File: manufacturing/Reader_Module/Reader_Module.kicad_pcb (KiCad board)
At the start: 4 copper layers, 30 x 70 mm, 49 parts, among them J1 SW-Debug, J2 Conn_01x04_Pin, SW1 NRST, U1 STM32L431KBU6, U2 SN65HVD230, U3 USBLC6-2, Y1 13.56MHz

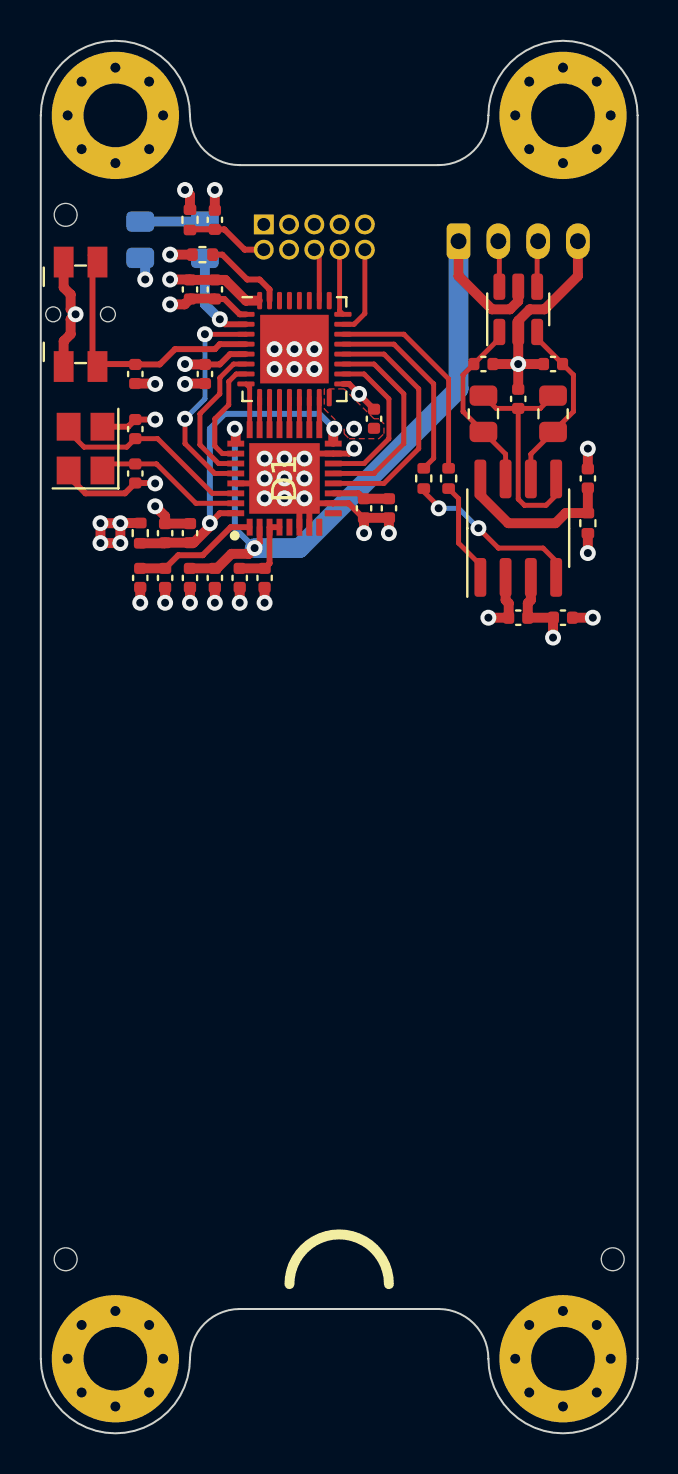
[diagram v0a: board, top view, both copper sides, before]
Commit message: Update PCB
Added Supplyline filtering
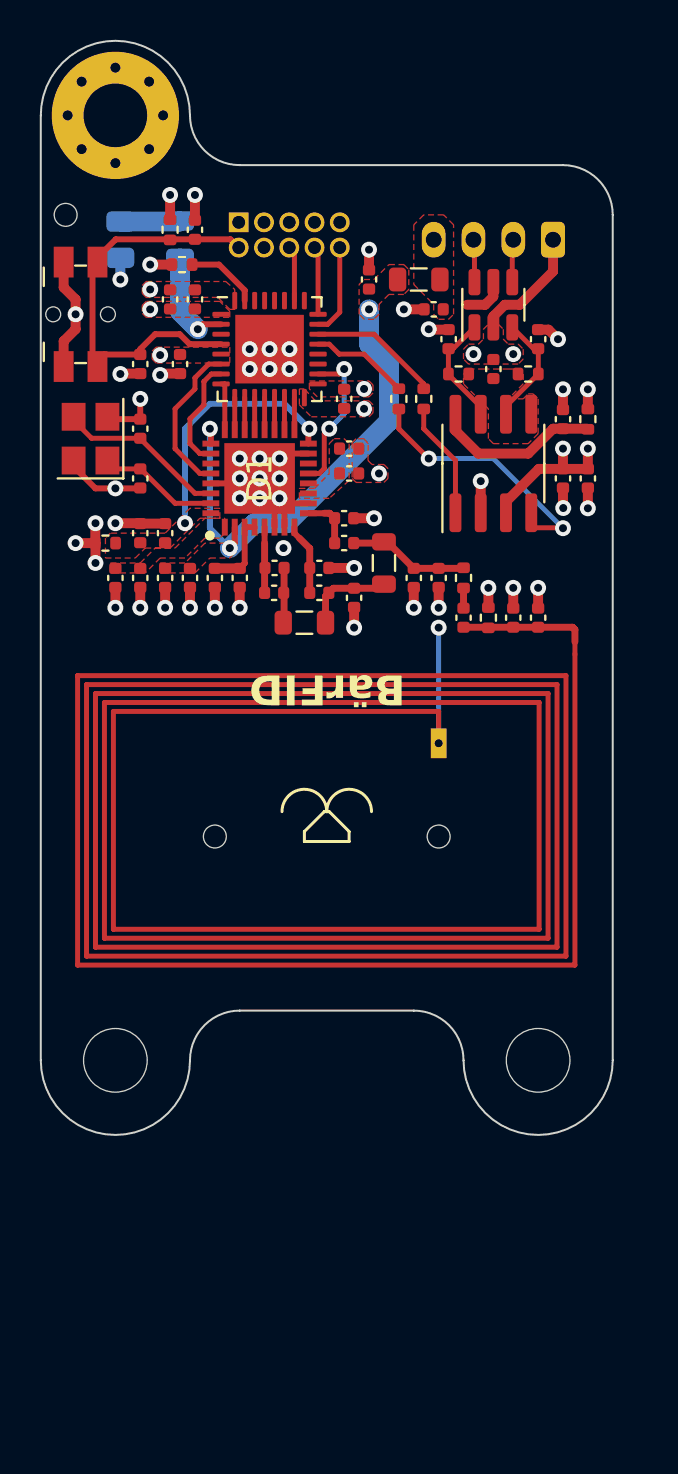
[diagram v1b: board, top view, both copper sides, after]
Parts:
- removed H2: MountingHole_Pad, MountingHole:MountingHole_3.2mm_M3_Pad_Via
- added AE1: Antenna_Loop, RF_Antenna:Custom_RFID_1, F.Cu at (109.3, 86.5)
- added C25: 47p, Capacitor_SMD:C_0402_1005Metric, F.Cu at (132.5, 84.0)
- added C26: 27p, Capacitor_SMD:C_0402_1005Metric, F.Cu at (131.2, 84.0)
- added C27: 68p, Capacitor_SMD:C_0402_1005Metric, F.Cu at (128.8, 84.0)
- added C28: 2u2, Capacitor_SMD:C_0402_1005Metric, F.Cu at (124.0, 67.0)
- added C29: 2u2, Capacitor_SMD:C_0402_1005Metric, F.Cu at (127.2, 68.5)
- added C30: 1n5, Capacitor_SMD:C_0402_1005Metric, F.Cu at (119.2, 81.5)
- added C31: 1n5, Capacitor_SMD:C_0402_1005Metric, F.Cu at (119.2, 82.8)
- added C32: 1n2, Capacitor_SMD:C_0402_1005Metric, F.Cu at (121.5, 82.8)
- added C33: 1n2, Capacitor_SMD:C_0402_1005Metric, F.Cu at (121.5, 81.5)
- added C34: 680p, Capacitor_SMD:C_0402_1005Metric, F.Cu at (123.2, 83.0)
- added C35: 220p, Capacitor_SMD:C_0402_1005Metric, F.Cu at (122.8, 80.2)
- added C36: 680p, Capacitor_SMD:C_0402_1005Metric, F.Cu at (122.8, 79.0)
- added C37: 100p, Capacitor_SMD:C_0402_1005Metric, F.Cu at (126.2, 82.0)
- added C38: 47p, Capacitor_SMD:C_0402_1005Metric, F.Cu at (127.5, 82.0)
- added FB2: 100 @ 100MHz, Inductor_SMD:L_0805_2012Metric, F.Cu at (126.5, 67.0)
- added G***: LOGO, Symbol:RFID-Gwent_M, B.Cu at (122.0, 98.5)
- added L1: 150n, Inductor_SMD:L_0805_2012Metric, F.Cu at (120.8, 84.2)
- added L2: 150n, Inductor_SMD:L_0805_2012Metric, F.Cu at (124.8, 81.2)
- added R10: 680R, Resistor_SMD:R_0402_1005Metric, F.Cu at (130.0, 84.0)
- added R11: 0R, Resistor_SMD:R_0402_1005Metric, F.Cu at (128.8, 82.0)
- H3, H4: footprint MountingHole:MountingHole_3.2mm_M3_Pad_Via -> MountingHole:MountingHole_3.2mm_M3
- J2: footprint Connector_Molex:Molex_Micro-Latch_53253-0470_1x04_P2.00mm_Vertical -> Connector_Molex:Molex_Micro-Latch_53254-0470_1x04_P2.00mm_Horizontal
- R6, R8: footprint Resistor_SMD:R_0805_2012Metric -> Resistor_SMD:R_0402_1005Metric
- moved H6 23.0 mm to (127.5, 95.0)
- moved H5 22.5 mm to (116.2, 95.0)
- moved H3 15.1 mm to (132.5, 106.2)
- moved H4 15.0 mm to (111.2, 106.2)
- moved C20 7.35 mm to (133.8, 77.0), turned to -90 degrees
- moved C19 7.11 mm to (135.0, 77.0), turned to -90 degrees
- moved R9 5.23 mm to (135.0, 74.0), turned to 90 degrees
- moved J2 4.75 mm to (133.2, 65.0), turned to 180 degrees
- moved R5 4.19 mm to (126.8, 73.0)
- moved R7 4.19 mm to (125.5, 73.0)
- moved C5 3.61 mm to (123.0, 75.5), turned to 180 degrees
- moved U2 3.48 mm to (130.2, 76.2)
- moved C24 3.23 mm to (133.8, 74.0)
- moved R6 2.36 mm to (128.5, 71.8), turned to 180 degrees
- moved R8 2.36 mm to (132.0, 71.8), turned to 180 degrees
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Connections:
- D1 pad 12: /MCU/TRF_ASK_OOK -> unconnected-(D1-ASK/OOK-Pad12)
- D1 pad 14: /MCU/TRF_MOD -> /TRF/TRF_MOD
- D1 pad 27: /MCU/TRF_SYS_CLK -> unconnected-(D1-SYS_CLK-Pad27)
- J2 pad 1: +5V -> GND
- J2 pad 2: /CAN/CAN_CON+ -> /CAN/CAN_CON-
- J2 pad 3: /CAN/CAN_CON- -> /CAN/CAN_CON+
- J2 pad 4: GND -> /CAN/CONN_5V
- U1 pad 18: /MCU/TRF_MOD -> /MCU/TRF_IRQ
- U1 pad 19: /MCU/TRF_IRQ -> unconnected-(U1-PA9-Pad19)
- U1 pad 20: /MCU/TRF_ASK_OOK -> unconnected-(U1-PA10-Pad20)
- U1 pad 3: /MCU/TRF_EN -> unconnected-(U1-PC15-Pad3)
- U1 pad 6: /MCU/TRF_SYS_CLK -> /MCU/TRF_EN
- U3 pad 5: +5V -> /CAN/CONN_5V
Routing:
- net +5V: track 39.9 -> 25.0 mm, vias 2 -> 3
- net /MCU/TRF_ASK_OOK: track 12.6 -> 0.00 mm
- net /CAN/VREF: track 11.7 -> 0.00 mm
- net +3V3: track 21.0 -> 12.7 mm
- net /MCU/TRF_MOD: track 8.15 -> 0.00 mm
- net /MCU/TRF_SYS_CLK: track 7.57 -> 0.00 mm
- net /TRF/VDD_A: track 6.36 -> 0.00 mm
- net /PCB Antenna/Antenna: track 0.00 -> 6.26 mm
- net Net-(C35-Pad2): track 0.00 -> 6.06 mm
- net /TRF/VDD_X: track 18.5 -> 12.8 mm
- net /CAN/CAN_RX: track 9.84 -> 4.99 mm
- net Net-(U2-R): track 9.04 -> 13.6 mm
- net Net-(C32-Pad2): track 0.00 -> 4.52 mm
- net /CAN/CAN_TX: track 10.6 -> 6.59 mm
- net /Matching NW/RF_RX_IN1: track 0.00 -> 3.62 mm
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- added copper zone on F.Cu, net +3V3
- added copper zone on F.Cu, net +5V
- added copper zone on F.Cu, net /CAN/CONN_5V
- added copper zone on F.Cu, net /CAN/VREF
- added copper zone on F.Cu, net /TRF/BG
- added copper zone on F.Cu, net /TRF/VDD_A
- added copper zone on F.Cu, net /TRF/VDD_X
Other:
- board size 30 x 70 mm -> 28.8 x 55 mm
- board text added: "-"
- board text added: "BärFID"

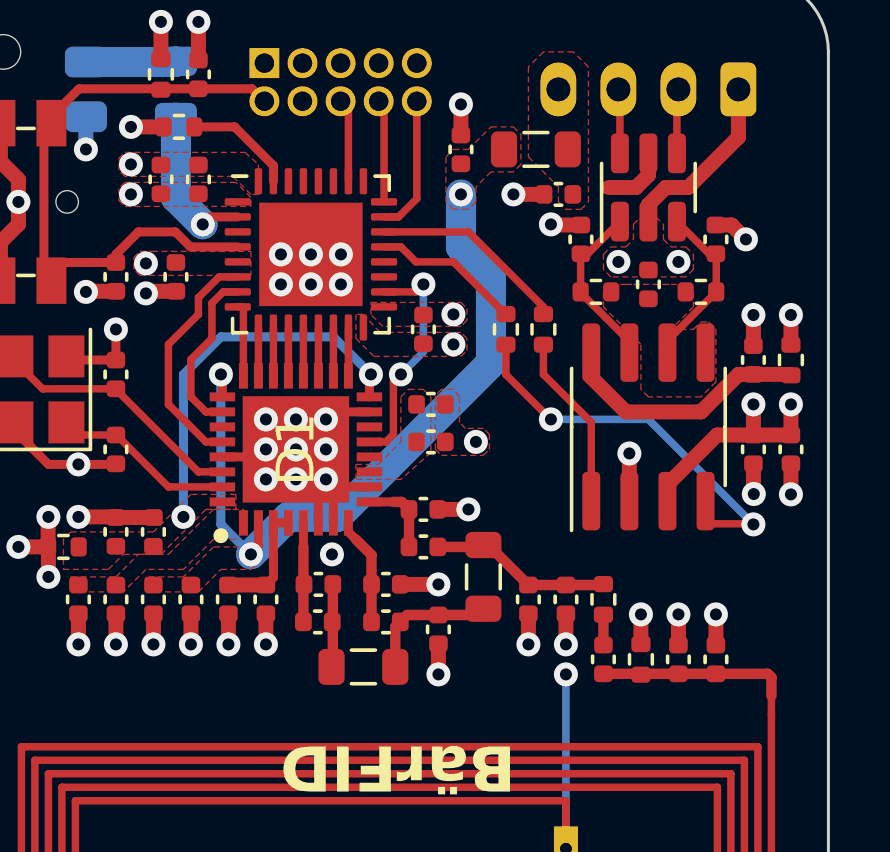
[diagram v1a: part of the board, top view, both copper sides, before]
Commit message: added PCB Images
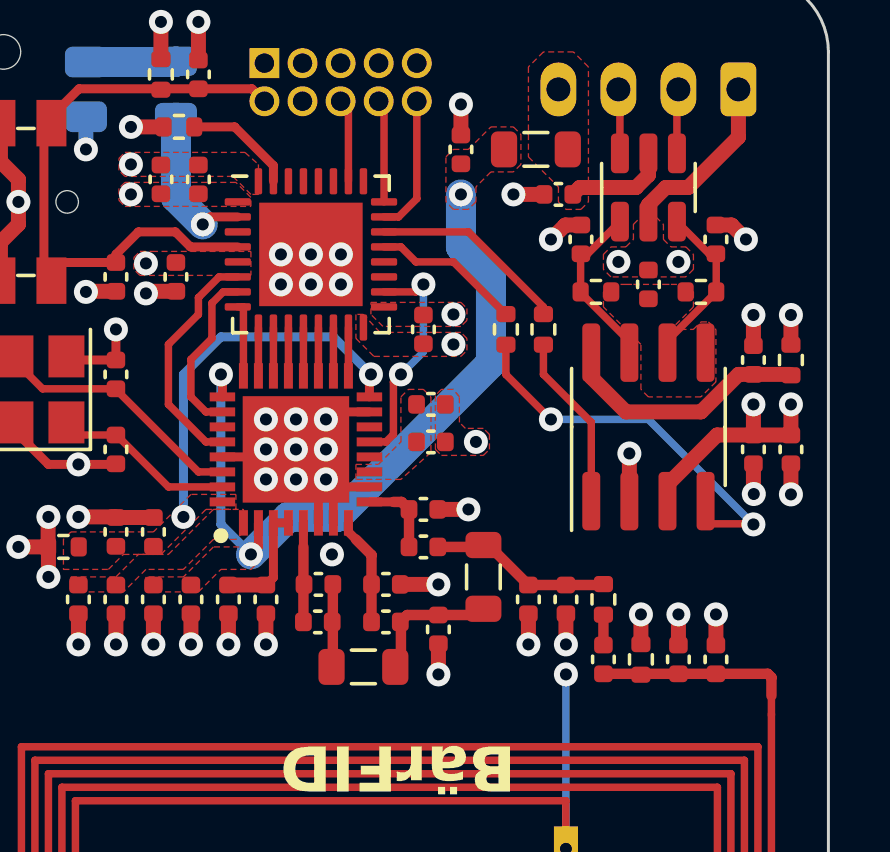
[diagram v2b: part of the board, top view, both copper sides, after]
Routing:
- net /CAN/CONN_5V: track 2.22 -> 3.51 mm
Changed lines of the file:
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@@
     (property "ki_description" "TRF7964A Multi Protocol Fully Integrated 13.56-MHz NFC / RFID Reader/Writer IC")
     (attr smd)
-    (fp_text reference "D1" (at 0 0 90) (layer "F.SilkS")
+    (fp_text reference "D1" (at 0 0 90) (layer "F.SilkS") hide
         (effects (font (size 1.27 1.27) (thickness 0.254)))
     )
@@
     )
   )
+  (segment (start 128 69.52) (end 127.48 69.52) (width 0.5) (layer "F.Cu") (net 1))
   (segment (start 135 77.48) (end 135 78.5) (width 0.5) (layer "F.Cu") (net 1))
   (segment (start 133.75 77.48) (end 133.75 78.474694) (width 0.5) (layer "F.Cu") (net 1))
@@
   (segment (start 132.5 83.52) (end 132.5 82.5) (width 0.5) (layer "F.Cu") (net 1))
   (segment (start 133.75 78.474694) (end 133.762653 78.487347) (width 0.5) (layer "F.Cu") (net 1))
-  (segment (start 127.020004 69.52) (end 127.000004 69.5) (width 0.5) (layer "F.Cu") (net 1))
   (segment (start 129.615 78.725) (end 129.615 77.135018) (width 0.5) (layer "F.Cu") (net 1))
-  (segment (start 132.5 69.52) (end 133.02 69.52) (width 0.5) (layer "F.Cu") (net 1))
   (segment (start 109.25 69.5) (end 109.25 68.75) (width 0.5) (layer "F.Cu") (net 1))
-  (segment (start 133.02 69.52) (end 133.5 70) (width 0.5) (layer "F.Cu") (net 1))
   (segment (start 120.95 75.75) (end 119.75 75.75) (width 0.3) (layer "F.Cu") (net 1))
   (segment (start 110.25 77.5) (end 109.15 76.4) (width 0.3) (layer "F.Cu") (net 1))
@@
   (segment (start 130 82.500016) (end 130.000016 82.5) (width 0.5) (layer "F.Cu") (net 1))
   (segment (start 115.25 64.02) (end 115.25 62.75) (width 0.5) (layer "F.Cu") (net 1))
+  (segment (start 127.48 69.52) (end 127 70) (width 0.5) (layer "F.Cu") (net 1))
   (segment (start 119.5 78) (end 118.5 77) (width 0.3) (layer "F.Cu") (net 1))
+  (segment (start 133.02 69.52) (end 133.5 70) (width 0.5) (layer "F.Cu") (net 1))
   (segment (start 130.826472 68.27) (end 131.573528 68.27) (width 0.5) (layer "F.Cu") (net 1))
   (segment (start 133.75 73.54) (end 133.75 72.52) (width 0.5) (layer "F.Cu") (net 1))
@@
   (segment (start 130 83.49) (end 130 82.500016) (width 0.5) (layer "F.Cu") (net 1))
   (segment (start 123.73 73.48) (end 123.75 73.5) (width 0.3) (layer "F.Cu") (net 1))
+  (segment (start 132.5 69.52) (end 133.02 69.52) (width 0.5) (layer "F.Cu") (net 1))
   (segment (start 113.570003 71.73) (end 113.5 71.800003) (width 0.5) (layer "F.Cu") (net 1))
   (segment (start 111.52 71.73) (end 111.5 71.75) (width 0.5) (layer "F.Cu") (net 1))
@@
   (segment (start 112.5 79.27) (end 112.48 79.25) (width 0.5) (layer "F.Cu") (net 1))
   (segment (start 109.15 76.4) (end 109.15 76.1) (width 0.3) (layer "F.Cu") (net 1))
-  (segment (start 128 69.52) (end 127.020004 69.52) (width 0.5) (layer "F.Cu") (net 1))
   (segment (start 126.25 82.48) (end 126.25 83.499974) (width 0.5) (layer "F.Cu") (net 1))
   (segment (start 133.25 66.593528) (end 133.25 65) (width 0.5) (layer "F.Cu") (net 1))
@@
   (via (at 118 71.5) (size 0.8) (drill 0.4) (layers "F.Cu" "B.Cu") (net 1))
   (via (at 124.5 76.75) (size 0.8) (drill 0.4) (layers "F.Cu" "B.Cu") (free) (net 1))
-  (via (at 133.5 70) (size 0.8) (drill 0.4) (layers "F.Cu" "B.Cu") (free) (net 1))
   (via (at 124 65.5) (size 0.8) (drill 0.4) (layers "F.Cu" "B.Cu") (free) (net 1))
   (via (at 116.25 83.5) (size 0.8) (drill 0.4) (layers "F.Cu" "B.Cu") (net 1))
   (via (at 119.7007 80.5) (size 0.8) (drill 0.4) (layers "F.Cu" "B.Cu") (free) (net 1))
   (via (at 126.250026 83.5) (size 0.8) (drill 0.4) (layers "F.Cu" "B.Cu") (free) (net 1))
+  (via (at 133.5 70) (size 0.8) (drill 0.4) (layers "F.Cu" "B.Cu") (net 1))
   (via (at 113.5 71.800003) (size 0.8) (drill 0.4) (layers "F.Cu" "B.Cu") (net 1))
   (via (at 123.75 73.5) (size 0.8) (drill 0.4) (layers "F.Cu" "B.Cu") (net 1))
@@
   (via (at 113 66.25) (size 0.8) (drill 0.4) (layers "F.Cu" "B.Cu") (net 1))
   (via (at 131.25 70.75) (size 0.8) (drill 0.4) (layers "F.Cu" "B.Cu") (free) (net 1))
-  (via (at 127.000004 69.5) (size 0.8) (drill 0.4) (layers "F.Cu" "B.Cu") (free) (net 1))
+  (via (at 127 70) (size 0.8) (drill 0.4) (layers "F.Cu" "B.Cu") (net 1))
   (via (at 125.75 68.5) (size 0.8) (drill 0.4) (layers "F.Cu" "B.Cu") (free) (net 1))
   (via (at 118.5 77) (size 0.8) (drill 0.4) (layers "F.Cu" "B.Cu") (net 1))
@@
   (segment (start 128.75 84.48) (end 134.23 84.48) (width 0.3493) (layer "F.Cu") (net 55))
   (segment (start 134.35 84.6) (end 134.35 85.2125) (width 0.3493) (layer "F.Cu") (net 55))
-  (segment (start 130.25 67.856522) (end 129.836523 68.27) (width 0.5) (layer "F.Cu") (net 56))
-  (segment (start 129.836523 68.27) (end 128.926472 68.27) (width 0.5) (layer "F.Cu") (net 56))
   (segment (start 130.25 67.1325) (end 130.25 67.856522) (width 0.5) (layer "F.Cu") (net 56))
+  (segment (start 127.96 68.27) (end 127.73 68.5) (width 0.5) (layer "F.Cu") (net 56))
+  (segment (start 130.25 67.856522) (end 129.836523 68.27) (width 0.5) (layer "F.Cu") (net 56))
+  (segment (start 129.836523 68.27) (end 127.96 68.27) (width 0.5) (layer "F.Cu") (net 56))
   (segment (start 119.73 81.5) (end 119.73 84.2075) (width 0.3493) (layer "F.Cu") (net 57))
   (segment (start 119.73 84.2075) (end 119.6875 84.25) (width 0.3493) (layer "F.Cu") (net 57))
-  (segment (start 121.8125 82.9175) (end 121.98 82.75) (width 0.3493) (layer "F.Cu") (net 58))
   (segment (start 124.5425 82.52) (end 124.75 82.3125) (width 0.3493) (layer "F.Cu") (net 58))
+  (segment (start 121.8125 84.25) (end 122 84.0625) (width 0.3493) (layer "F.Cu") (net 58))
   (segment (start 123.25 82.52) (end 124.5425 82.52) (width 0.3493) (layer "F.Cu") (net 58))
-  (segment (start 121.8125 84.25) (end 121.8125 82.9175) (width 0.3493) (layer "F.Cu") (net 58))
   (segment (start 121.98 82.75) (end 122.21 82.52) (width 0.3493) (layer "F.Cu") (net 58))
   (segment (start 122.21 82.52) (end 123.25 82.52) (width 0.3493) (layer "F.Cu") (net 58))
+  (segment (start 122 82.77) (end 121.98 82.75) (width 0.3493) (layer "F.Cu") (net 58))
+  (segment (start 122 84.0625) (end 122 82.77) (width 0.3493) (layer "F.Cu") (net 58))
   (segment (start 126.25 81.52) (end 128.72 81.52) (width 0.3493) (layer "F.Cu") (net 59))
   (segment (start 123.23 80.25) (end 124.98 80.25) (width 0.3493) (layer "F.Cu") (net 59))
@@
         (xy 110.5 78.25)
         (xy 108 78.25)
-        (xy 108 85.75)
-        (xy 135.75 85.75)
+        (xy 108 85.25)
+        (xy 135.75 85.25)
         (xy 135.75 64)
         (xy 133.5 61.75)
@@
         (xy 110.5 78.25)
         (xy 108 78.25)
-        (xy 108 85)
-        (xy 135.5 85)
-        (xy 135.5 58.75)
-        (xy 131.25 58.75)
-        (xy 129 61.75)
-        (xy 116 61.75)
-        (xy 113.75 58.75)
+        (xy 108 85.25)
+        (xy 135.75 85.25)
+        (xy 135.75 64)
+        (xy 133.5 61.75)
+        (xy 114.5 61.75)
+        (xy 114.5 58.75)
         (xy 108 58.75)
       )

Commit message: upd board
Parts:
- removed H1: MountingHole_Pad, MountingHole:MountingHole_3.2mm_M3_Pad_Via
- C17, C18: value 27pF -> 27p
- C30: value 1n5 -> 1n2
- C31: value 1n5 -> 1n8
- C7: value 1u -> 2u2
- R2: value 1k -> 1k5
- R5, R7: value 47R -> 56R
- moved H7 0.50 mm to (109.2, 63.8)
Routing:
- net +3V3: track 12.7 -> 0.08 mm
- net GND: track 70.5 -> 73.0 mm, vias 53 -> 56
- net +5V: track 25.0 -> 26.0 mm
- added copper zone on B.Cu, net +3V3
- added copper zone on In2.Cu, net GND
- removed copper zone on In2.Cu, net +3V3
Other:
- board size 28.8 x 55 mm -> 28.8 x 48.8 mm
